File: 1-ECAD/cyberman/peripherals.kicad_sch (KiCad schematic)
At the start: 26 parts, among them J1 5033981892, SW1 SKRMAAE010, SW2 SKRMAAE010, SW3 SKRMAAE010, SW4 SKRMAAE010, SW5 SKRMAAE010, SW6 SKRMAAE010, U18 PM254-2-10-W-8.5

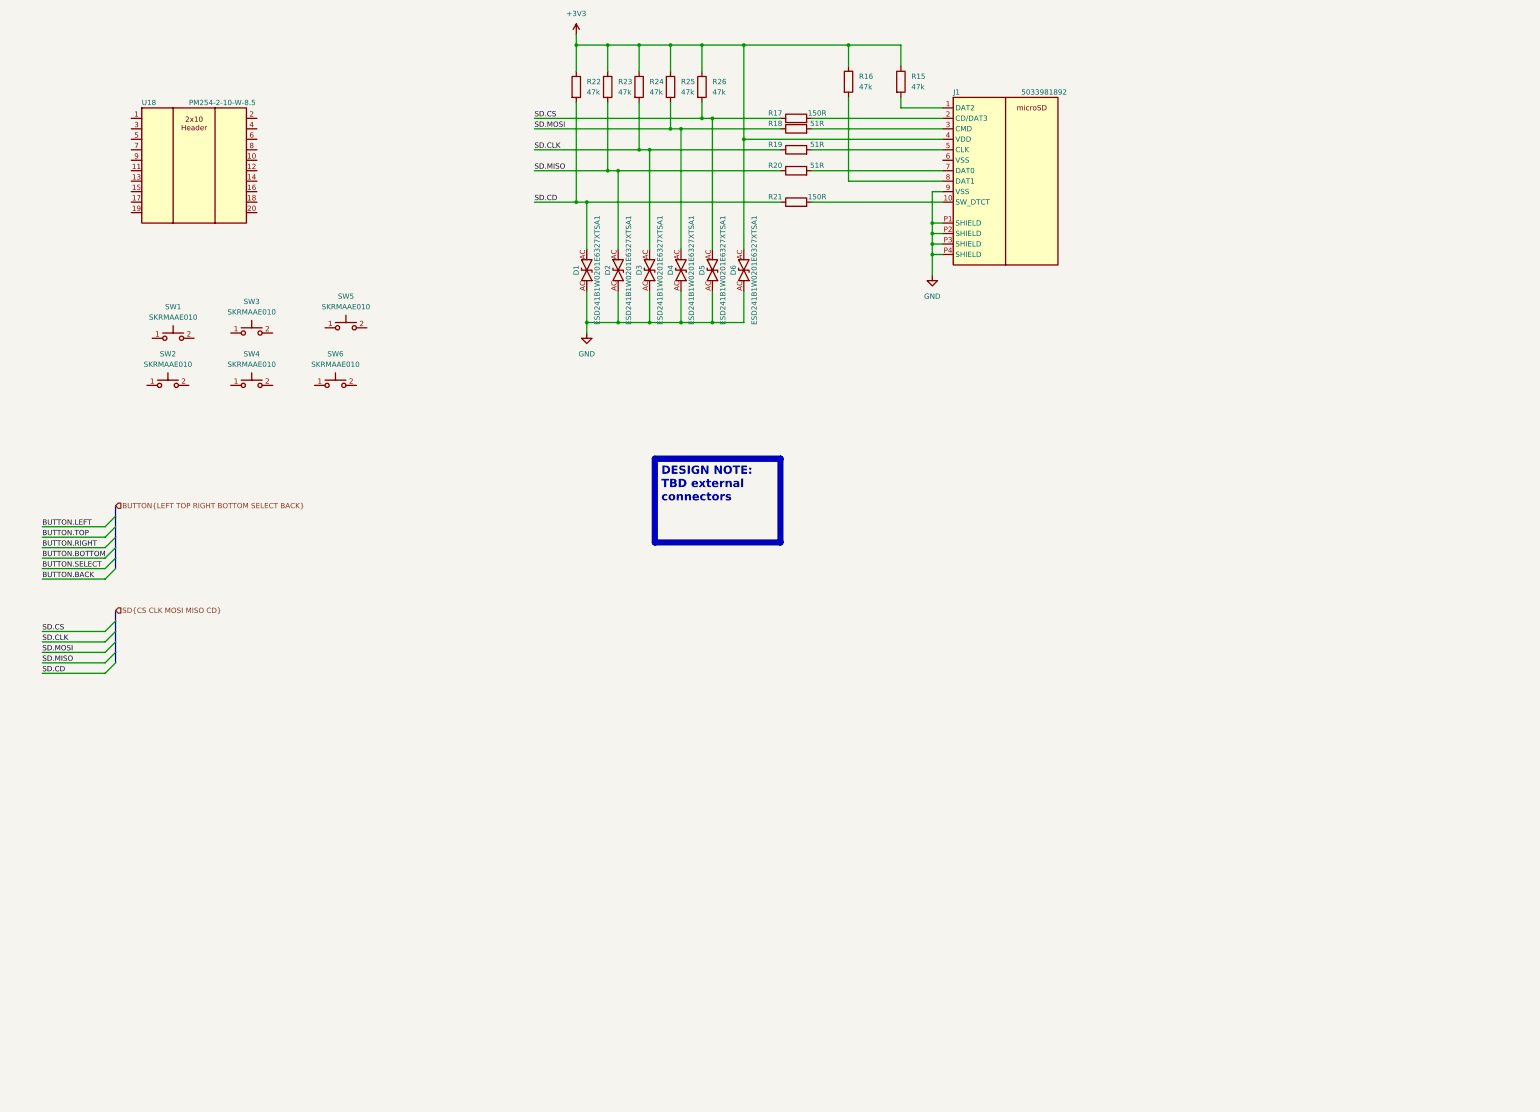
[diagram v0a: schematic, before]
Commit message: new changes
close display page and peripheral schematic
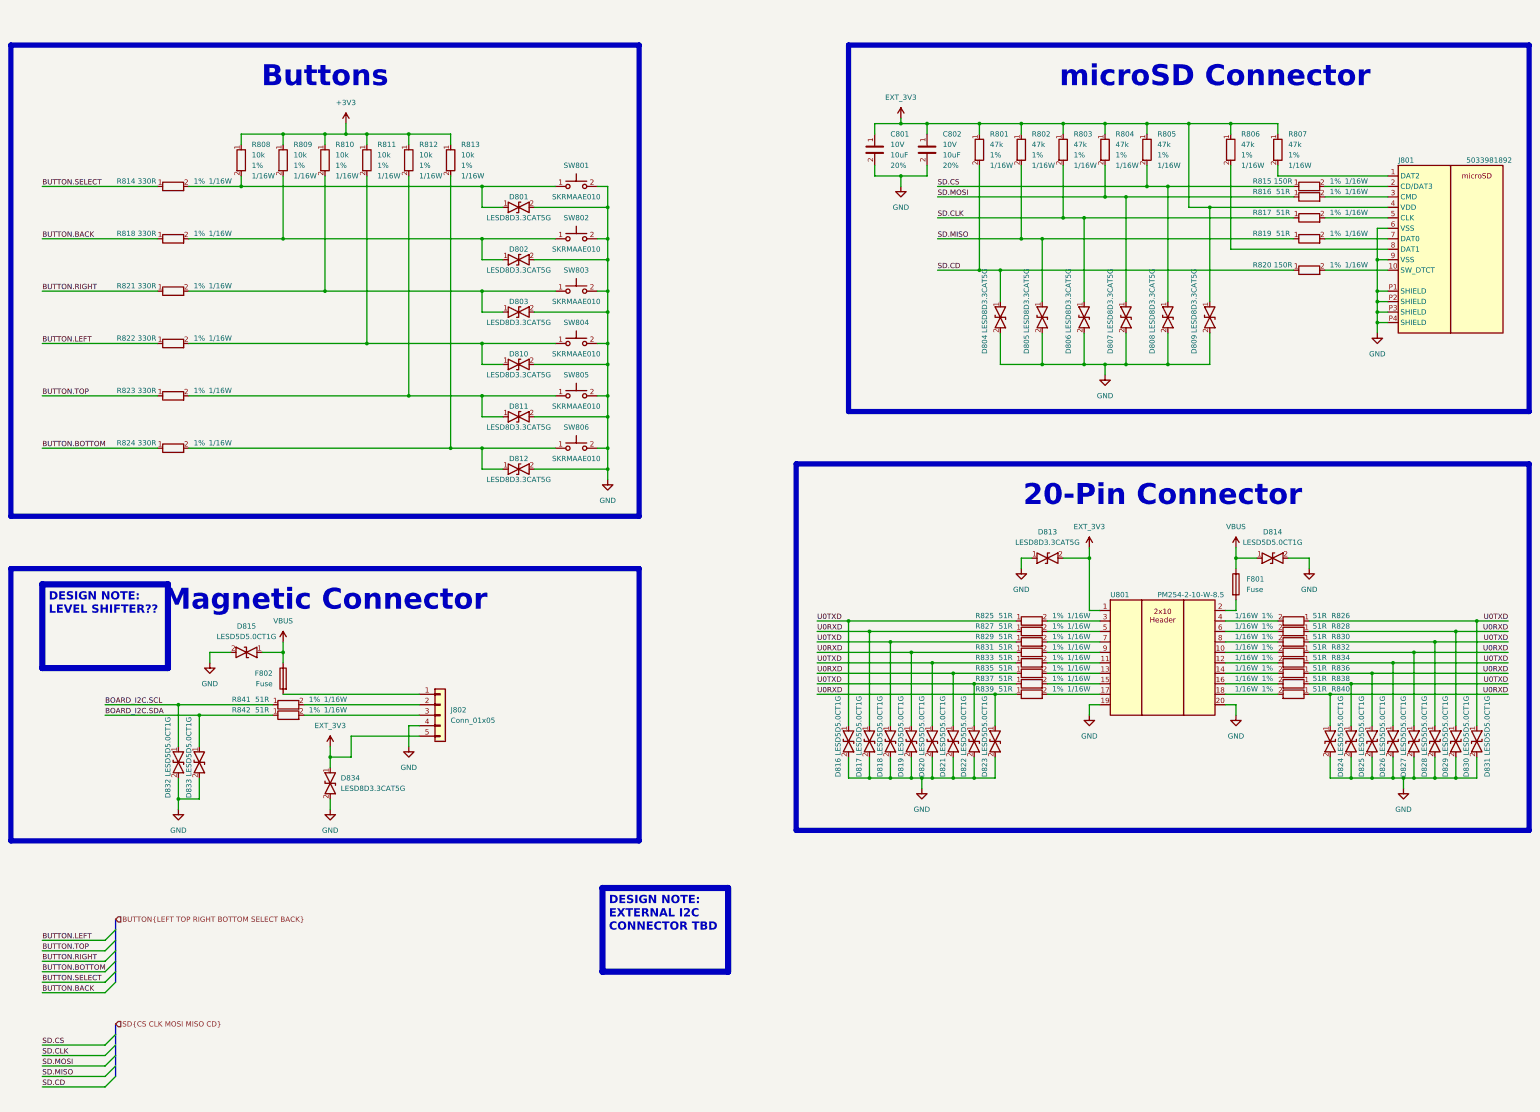
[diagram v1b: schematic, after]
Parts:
- removed D1, D2, D3, D4, D5, D6: ESD241B1W0201E6327XTSA1, symbol 0_diode:ESD241B1W0201E6327XTSA1
- removed R15, R16, R22, R23, R24, R25, R26: 47k, symbol Device:R
- removed R17, R21: 150R, symbol Device:R
- removed R18, R19, R20: 51R, symbol Device:R
- removed SW1, SW2, SW3, SW4, SW5, SW6: SKRMAAE010, 0_switch:SKRMAAE010, symbol 0_switch:SKRMAAE010
- added C801, C802: CC0402MRX5R6BB106, 0_capacitor_smd:C_0402, symbol 0_capacitor_smd:CC0402MRX5R6BB106
- added D801, D802, D803, D804, D805, D806, D807, D808, D809, D810, D811, D812, D813, D834: LESD8D3.3CAT5G, 0_diode_smd:LESD8D3.3CAT5G, symbol 0_diode:LESD8D3.3CAT5G
- added D814, D815, D816, D817, D818, D819, D820, D821, D822, D823, D824, D825, D826, D827, D828, D829, D830, D831, D832, D833: LESD5D5.0CT1G, 0_diode_smd:LESD5D5.0CT1G, symbol 0_diode:LESD5D5.0CT1G
- added F801, F802: Fuse, symbol Device:Fuse
- added J802: Conn_01x05, symbol Connector_Generic:Conn_01x05
- added R801, R802, R803, R804, R805, R806, R807: RC0402FR-0747KL, 0_resistor_smd:R_0402, symbol 0_resistor_smd:RC0402FR-0747KL
- added R808, R809, R810, R811, R812, R813: RC0402FR-0710KL, 0_resistor_smd:R_0402, symbol 0_resistor_smd:RC0402FR-0710KL
- added R814, R818, R821, R822, R823, R824: RC0402FR-07330RL, 0_resistor_smd:R_0402, symbol 0_resistor_smd:RC0402FR-07330RL
- added R815, R820: RC0402FR-07150RL, 0_resistor_smd:R_0402, symbol 0_resistor_smd:RC0402FR-07150RL
- added R816, R817, R819, R825, R826, R827, R828, R829, R830, R831, R832, R833, R834, R835, R836, R837, R838, R839, R840, R841, R842: RC0402FR-0751RL, 0_resistor_smd:R_0402, symbol 0_resistor_smd:RC0402FR-0751RL
- added SW801, SW802, SW803, SW804, SW805, SW806: SKRMAAE010, 0_switch:SKRMAAE010, symbol 0_switch:SKRMAAE010
- renumbered J1 to J801, U18 to U801
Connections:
- net +3V3: now also R808.1, R809.1, R810.1, R811.1, R812.1, R813.1; no longer J801.4 (VDD)
- net BUTTON.BACK: now also R818.1
- net BUTTON.BOTTOM: now also R824.1
- net BUTTON.LEFT: now also R822.1
- net BUTTON.RIGHT: now also R821.1
- net BUTTON.SELECT: now also R814.1
- net BUTTON.TOP: now also R823.1
- net GND: now also J801.6 (VSS), U801.19, U801.20, C801.2, C802.2, D801.2, D802.2, D803.2, D804.2, D805.2, D806.2, D807.2, D808.2, D809.2, D810.2, D811.2, D812.2, D813.1, D814.2, D815.2, D816.2, D817.2, D818.2, D819.2, D820.2, D821.2, D822.2, D823.2, D824.2, D825.2, D826.2, D827.2, D828.2, D829.2, D830.2, D831.2, D832.2, D833.2, D834.2, J802.4 (Pin_4), SW801.2, SW802.2, SW803.2, SW804.2, SW805.2, SW806.2
- net SD.CD: now also D804.1, R801.2, R820.1
- net SD.CLK: now also D806.1, R803.2, R817.1
- net SD.CS: now also D808.1, R805.2, R815.1
- net SD.MISO: now also D805.1, R802.2, R819.1
- net SD.MOSI: now also D807.1, R804.2, R816.1
- net at J801.1 (DAT2): now also R807.2
- net at J801.7 (DAT0): now also R819.2
- net at J801.5 (CLK): now also R817.2
- net at J801.3 (CMD): now also R816.2
- net EXT_3V3: now reaches U801.1
- net EXT_3V3: now also J801.4 (VDD), C801.1, C802.1, D809.1, D813.2, D834.1, J802.5 (Pin_5), R801.1, R802.1, R803.1, R804.1, R805.1, R806.1, R807.1
- net at U801.10: now also R832.2
- net at U801.11: now also R833.2
- net at U801.12: now also R834.2
- net at U801.13: now also R835.2
- net at U801.14: now also R836.2
- net at U801.15: now also R837.2
- net at U801.16: now also R838.2
- net at U801.17: now also R839.2
- net at U801.18: now also R840.2
- net at U801.2: now also F801.2
- net at U801.3: now also R825.2
- net at U801.4: now also R826.2
- net at U801.5: now also R827.2
- net at U801.6: now also R828.2
- net at U801.7: now also R829.2
- net at U801.8: now also R830.2
- net at U801.9: now also R831.2
- net at J801.10 (SW_DTCT): now also R820.2
- net at J801.8 (DAT1): now also R806.2
- net at J801.2 (CD/DAT3): now also R815.2
- new net: D802.1, R809.2, R818.2, SW802.1
- new net: D803.1, R810.2, R821.2, SW803.1
- new net: D810.1, R811.2, R822.2, SW804.1
- new net: D801.1, R808.2, R814.2, SW801.1
- new net: J802.3 (Pin_3), R842.2
- new net: J802.2 (Pin_2), R841.2
- new net: D812.1, R813.2, R824.2, SW806.1
- new net: D811.1, R812.2, R823.2, SW805.1
- new net: F802.2, J802.1 (Pin_1)
- new net BOARD_I2C.SCL: D832.1, R841.1
- new net BOARD_I2C.SDA: D833.1, R842.1
- new net U0RXD: D817.1, D819.1, D821.1, D823.1, D824.1, D826.1, D828.1, D830.1, R827.1, R828.1, R831.1, R832.1, R835.1, R836.1, R839.1, R840.1
- new net U0TXD: D816.1, D818.1, D820.1, D822.1, D825.1, D827.1, D829.1, D831.1, R825.1, R826.1, R829.1, R830.1, R833.1, R834.1, R837.1, R838.1
- new net VBUS: D814.1, D815.1, F801.1, F802.1
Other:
- note added: "20-Pin Connector"
- note added: "Buttons"
- note added: "Magnetic Connector"
- note added: "microSD Connector"
- company: (none) -> kode.
- title: (none) -> Peripherals
- moved on the sheet: J801, U801

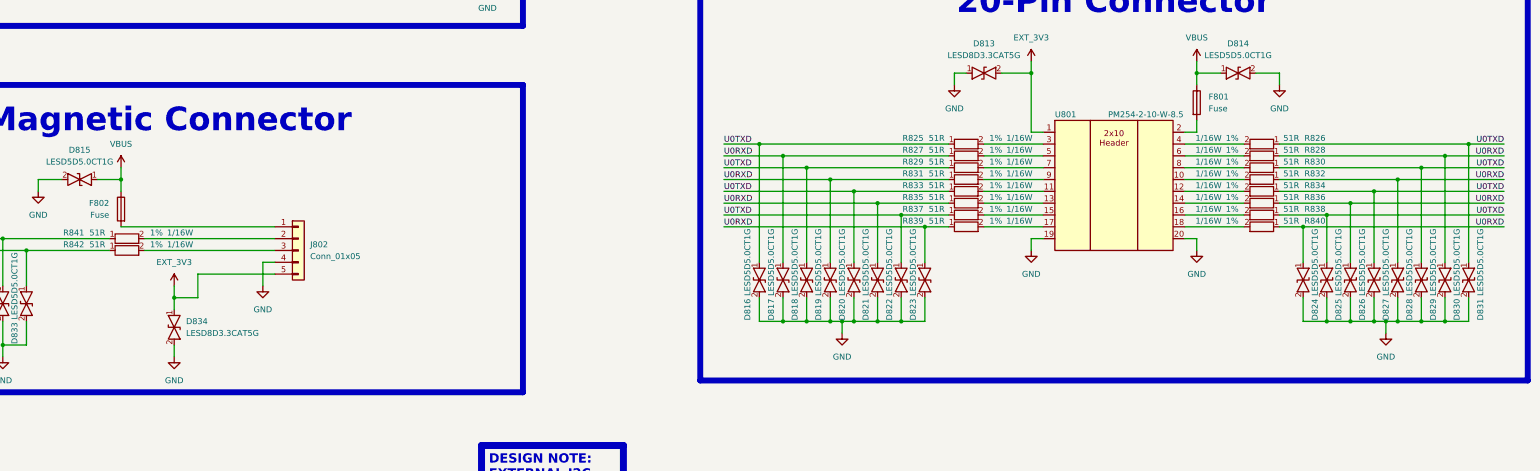
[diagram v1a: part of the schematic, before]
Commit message: add fuse and place external connector
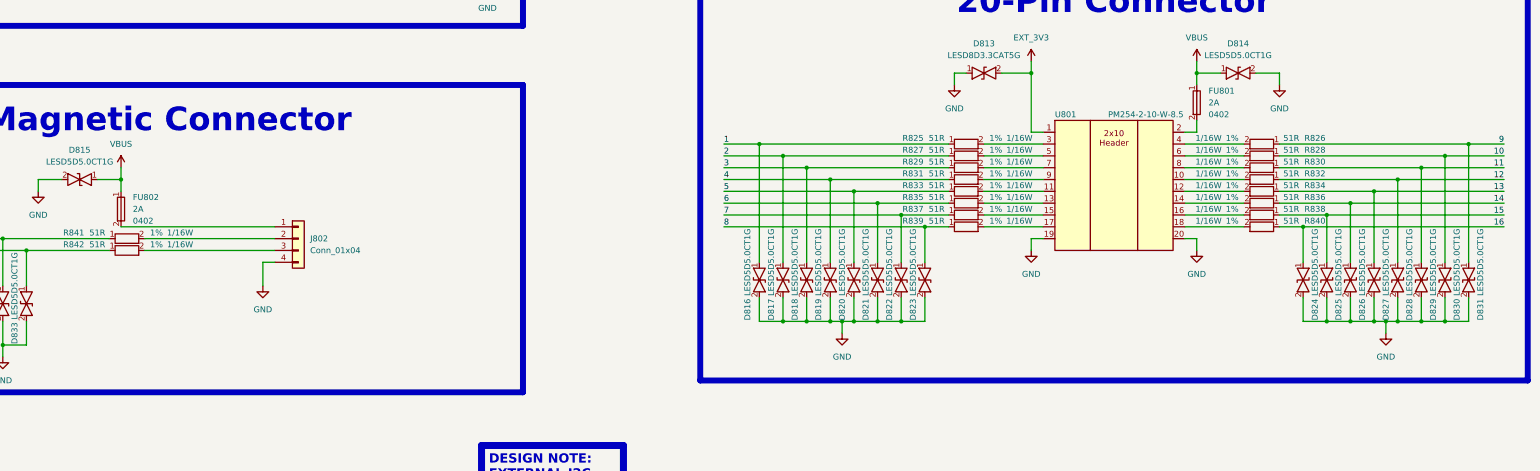
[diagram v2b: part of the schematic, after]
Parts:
- removed D834: LESD8D3.3CAT5G, 0_diode_smd:LESD8D3.3CAT5G, symbol 0_diode:LESD8D3.3CAT5G
- removed F801, F802: Fuse, symbol Device:Fuse
- removed J802: Conn_01x05, symbol Connector_Generic:Conn_01x05
- added FU801, FU802: ERBRD2R00X, 0_fuses_smd:ERBRD0R63X, symbol 0_fuse_smd:ERBRD2R00X
- added J802: Conn_01x04, symbol Connector_Generic:Conn_01x04
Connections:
- net GND: now also J802.4 (Pin_4)
- net VBUS: now also FU801.1, FU802.1
- net at R842.2: now also J802.3 (Pin_3)
- net at R841.2: now also J802.2 (Pin_2)
- net at U801.2: now also FU801.2
- removed net U0RXD: D817.1, D819.1, D821.1, D823.1, D824.1, D826.1, D828.1, D830.1, R827.1, R828.1, R831.1, R832.1, R835.1, R836.1, R839.1, R840.1
- removed net U0TXD: D816.1, D818.1, D820.1, D822.1, D825.1, D827.1, D829.1, D831.1, R825.1, R826.1, R829.1, R830.1, R833.1, R834.1, R837.1, R838.1
- new net: FU802.2, J802.1 (Pin_1)
- new net 1: D816.1, R825.1
- new net 10: D830.1, R828.1
- new net 11: D829.1, R830.1
- new net 12: D828.1, R832.1
- new net 13: D827.1, R834.1
- new net 14: D826.1, R836.1
- new net 15: D825.1, R838.1
- new net 16: D824.1, R840.1
- new net 2: D817.1, R827.1
- new net 3: D818.1, R829.1
- new net 4: D819.1, R831.1
- new net 5: D820.1, R833.1
- new net 6: D821.1, R835.1
- new net 7: D822.1, R837.1
- new net 8: D823.1, R839.1
- new net 9: D831.1, R826.1

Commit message: change layout
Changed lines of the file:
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@@
 	)
 	(bus_entry
-		(at 50.8 275.59)
+		(at 50.8 279.4)
 		(size -2.54 2.54)
 		(stroke
@@
 	)
 	(bus_entry
-		(at 50.8 265.43)
+		(at 50.8 269.24)
 		(size -2.54 2.54)
 		(stroke
@@
 	)
 	(bus_entry
-		(at 50.8 240.03)
+		(at 50.8 243.84)
 		(size -2.54 2.54)
 		(stroke
@@
 	)
 	(bus_entry
-		(at 50.8 242.57)
+		(at 50.8 246.38)
 		(size -2.54 2.54)
 		(stroke
@@
 	)
 	(bus_entry
-		(at 50.8 245.11)
+		(at 50.8 248.92)
 		(size -2.54 2.54)
 		(stroke
@@
 	)
 	(bus_entry
-		(at 50.8 250.19)
+		(at 50.8 254)
 		(size -2.54 2.54)
 		(stroke
@@
 	)
 	(bus_entry
-		(at 50.8 273.05)
+		(at 50.8 276.86)
 		(size -2.54 2.54)
 		(stroke
@@
 	)
 	(bus_entry
-		(at 50.8 252.73)
+		(at 50.8 256.54)
 		(size -2.54 2.54)
 		(stroke
@@
 	)
 	(bus_entry
-		(at 50.8 270.51)
+		(at 50.8 274.32)
 		(size -2.54 2.54)
 		(stroke
@@
 	)
 	(bus_entry
-		(at 50.8 267.97)
+		(at 50.8 271.78)
 		(size -2.54 2.54)
 		(stroke
@@
 	)
 	(bus_entry
-		(at 50.8 247.65)
+		(at 50.8 251.46)
 		(size -2.54 2.54)
 		(stroke
@@
 	(wire
 		(pts
-			(xy 33.02 273.05) (xy 48.26 273.05)
+			(xy 33.02 276.86) (xy 48.26 276.86)
 		)
 		(stroke
@@
 	(bus
 		(pts
-			(xy 50.8 270.51) (xy 50.8 273.05)
+			(xy 50.8 274.32) (xy 50.8 276.86)
 		)
 		(stroke
@@
 	(wire
 		(pts
-			(xy 33.02 247.65) (xy 48.26 247.65)
+			(xy 33.02 251.46) (xy 48.26 251.46)
 		)
 		(stroke
@@
 	(wire
 		(pts
-			(xy 33.02 252.73) (xy 48.26 252.73)
+			(xy 33.02 256.54) (xy 48.26 256.54)
 		)
 		(stroke
@@
 	(bus
 		(pts
-			(xy 50.8 237.49) (xy 50.8 240.03)
+			(xy 50.8 241.3) (xy 50.8 243.84)
 		)
 		(stroke
@@
 	(wire
 		(pts
-			(xy 33.02 242.57) (xy 48.26 242.57)
+			(xy 33.02 246.38) (xy 48.26 246.38)
 		)
 		(stroke
@@
 	(wire
 		(pts
-			(xy 33.02 275.59) (xy 48.26 275.59)
+			(xy 33.02 279.4) (xy 48.26 279.4)
 		)
 		(stroke
@@
 	(bus
 		(pts
-			(xy 50.8 245.11) (xy 50.8 247.65)
+			(xy 50.8 248.92) (xy 50.8 251.46)
 		)
 		(stroke
@@
 	(bus
 		(pts
-			(xy 50.8 265.43) (xy 50.8 267.97)
+			(xy 50.8 269.24) (xy 50.8 271.78)
 		)
 		(stroke
@@
 	(wire
 		(pts
-			(xy 33.02 270.51) (xy 48.26 270.51)
+			(xy 33.02 274.32) (xy 48.26 274.32)
 		)
 		(stroke
@@
 	(bus
 		(pts
-			(xy 50.8 247.65) (xy 50.8 250.19)
+			(xy 50.8 251.46) (xy 50.8 254)
 		)
 		(stroke
@@
 	(wire
 		(pts
-			(xy 33.02 267.97) (xy 48.26 267.97)
+			(xy 33.02 271.78) (xy 48.26 271.78)
 		)
 		(stroke
@@
 	(wire
 		(pts
-			(xy 33.02 250.19) (xy 48.26 250.19)
+			(xy 33.02 254) (xy 48.26 254)
 		)
 		(stroke
@@
 	(wire
 		(pts
-			(xy 33.02 255.27) (xy 48.26 255.27)
+			(xy 33.02 259.08) (xy 48.26 259.08)
 		)
 		(stroke
@@
 	(bus
 		(pts
-			(xy 50.8 273.05) (xy 50.8 275.59)
+			(xy 50.8 276.86) (xy 50.8 279.4)
 		)
 		(stroke
@@
 	(bus
 		(pts
-			(xy 50.8 262.89) (xy 50.8 265.43)
+			(xy 50.8 266.7) (xy 50.8 269.24)
 		)
 		(stroke
@@
 	(wire
 		(pts
-			(xy 33.02 245.11) (xy 48.26 245.11)
+			(xy 33.02 248.92) (xy 48.26 248.92)
 		)
 		(stroke
@@
 	(bus
 		(pts
-			(xy 50.8 240.03) (xy 50.8 242.57)
+			(xy 50.8 243.84) (xy 50.8 246.38)
 		)
 		(stroke
@@
 	(bus
 		(pts
-			(xy 50.8 242.57) (xy 50.8 245.11)
+			(xy 50.8 246.38) (xy 50.8 248.92)
 		)
 		(stroke
@@
 	(bus
 		(pts
-			(xy 50.8 267.97) (xy 50.8 270.51)
+			(xy 50.8 271.78) (xy 50.8 274.32)
 		)
 		(stroke
@@
 	(bus
 		(pts
-			(xy 50.8 250.19) (xy 50.8 252.73)
+			(xy 50.8 254) (xy 50.8 256.54)
 		)
 		(stroke
@@
 	(wire
 		(pts
-			(xy 33.02 278.13) (xy 48.26 278.13)
+			(xy 33.02 281.94) (xy 48.26 281.94)
 		)
 		(stroke
@@
 	(text_box "DESIGN NOTE:\nEXTERNAL I2C CONNECTOR TBD"
 		(exclude_from_sim no)
-		(at 168.91 229.87 0)
+		(at 140.97 165.1 0)
 		(size 30.48 20.32)
 		(stroke
@@
 	)
 	(label "BUTTON.LEFT"
-		(at 33.02 242.57 0)
+		(at 33.02 246.38 0)
 		(fields_autoplaced yes)
 		(effects
@@
 	)
 	(label "SD.MOSI"
-		(at 33.02 273.05 0)
+		(at 33.02 276.86 0)
 		(fields_autoplaced yes)
 		(effects
@@
 	)
 	(label "SD.MISO"
-		(at 33.02 275.59 0)
+		(at 33.02 279.4 0)
 		(fields_autoplaced yes)
 		(effects
@@
 	)
 	(label "BUTTON.BACK"
-		(at 33.02 255.27 0)
+		(at 33.02 259.08 0)
 		(fields_autoplaced yes)
 		(effects
@@
 	)
 	(label "BUTTON.TOP"
-		(at 33.02 245.11 0)
+		(at 33.02 248.92 0)
 		(fields_autoplaced yes)
 		(effects
@@
 	)
 	(label "BUTTON.RIGHT"
-		(at 33.02 247.65 0)
+		(at 33.02 251.46 0)
 		(fields_autoplaced yes)
 		(effects
@@
 	)
 	(label "BUTTON.SELECT"
-		(at 33.02 252.73 0)
+		(at 33.02 256.54 0)
 		(fields_autoplaced yes)
 		(effects
@@
 	)
 	(label "SD.CD"
-		(at 33.02 278.13 0)
+		(at 33.02 281.94 0)
 		(fields_autoplaced yes)
 		(effects
@@
 	)
 	(label "BUTTON.BOTTOM"
-		(at 33.02 250.19 0)
+		(at 33.02 254 0)
 		(fields_autoplaced yes)
 		(effects
@@
 	)
 	(label "SD.CS"
-		(at 33.02 267.97 0)
+		(at 33.02 271.78 0)
 		(fields_autoplaced yes)
 		(effects
@@
 	)
 	(label "SD.CLK"
-		(at 33.02 270.51 0)
+		(at 33.02 274.32 0)
 		(fields_autoplaced yes)
 		(effects
@@
 	(hierarchical_label "SD{CS CLK MOSI MISO CD}"
 		(shape input)
-		(at 50.8 262.89 0)
+		(at 50.8 266.7 0)
 		(fields_autoplaced yes)
 		(effects
@@
 	(hierarchical_label "BUTTON{LEFT TOP RIGHT BOTTOM SELECT BACK}"
 		(shape input)
-		(at 50.8 237.49 0)
+		(at 50.8 241.3 0)
 		(fields_autoplaced yes)
 		(effects
